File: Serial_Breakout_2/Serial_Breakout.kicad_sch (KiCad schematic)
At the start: 3 parts, among them J1 VIC Serial In, J2 Disc Serial Out, J3 Breakout

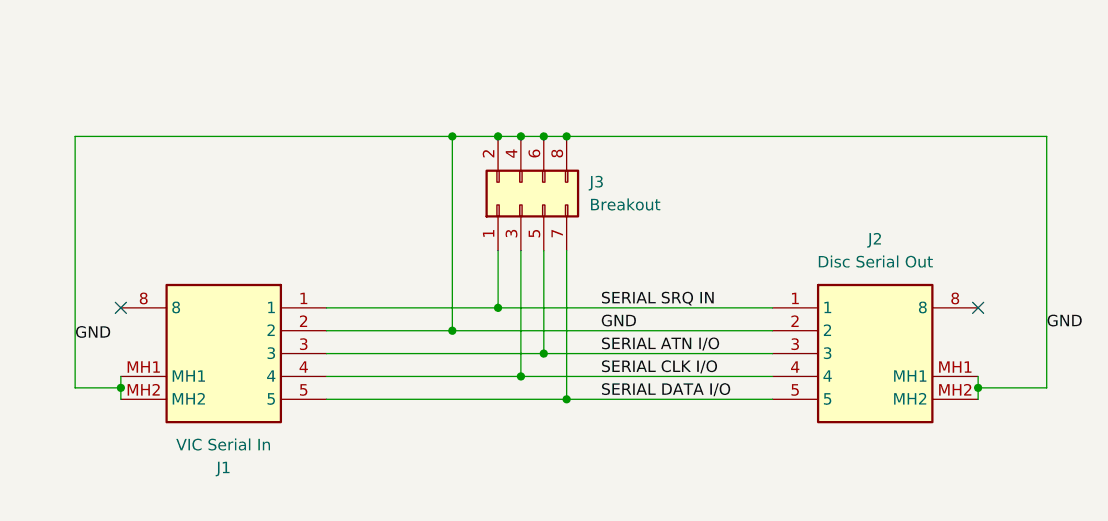
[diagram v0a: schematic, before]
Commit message: Corrected pinout
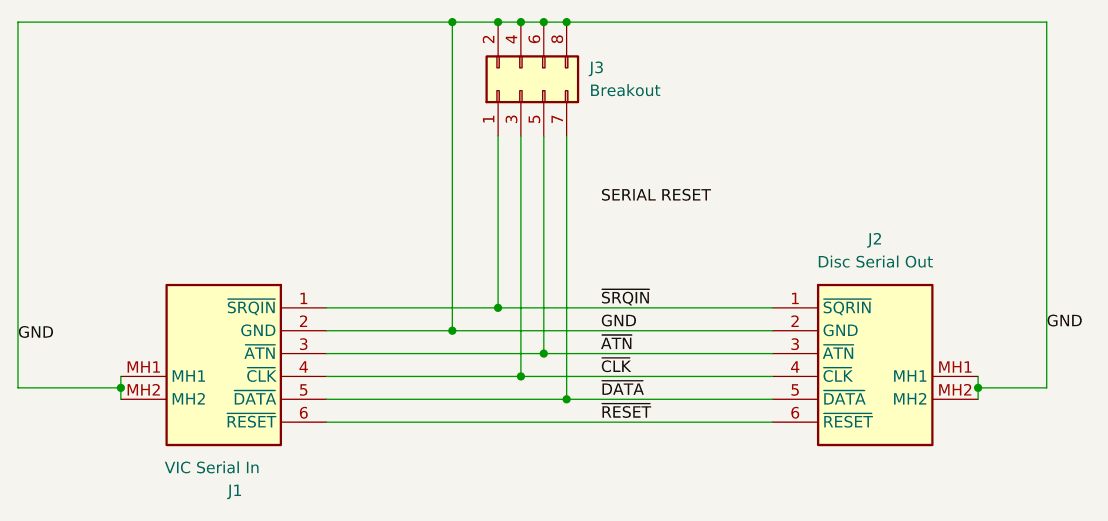
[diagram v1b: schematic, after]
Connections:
- net SERIAL ATN I/O renamed ~{ATN}
- net SERIAL CLK I/O renamed ~{CLK}
- net SERIAL DATA I/O renamed ~{DATA}
- net SERIAL SRQ IN renamed ~{SRQIN}
- new net ~{RESET}: J1.6 (~{RESET}), J2.6 (~{RESET})
- no-connect marks 2 -> 0
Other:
- moved on the sheet: J1, J2, J3
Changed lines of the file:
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@@
 	(title_block
 		(title "Breakout Board for Commodore Serial Port")
-		(date "23/NOV/2025")
-		(rev "B")
+		(date "22/FEB/2026")
+		(rev "C")
 		(company "www.youtube.com/@Brfff")
 	)
@@
 	)
 	(junction
-		(at 82.55 38.1)
-		(diameter 0)
-		(color 0 0 0 0)
-	)
-	(junction
-		(at 85.09 38.1)
-		(diameter 0)
-		(color 0 0 0 0)
-	)
-	(junction
-		(at 77.47 38.1)
-		(diameter 0)
-		(color 0 0 0 0)
-	)
-	(junction
-		(at 90.17 38.1)
+		(at 82.55 25.4)
+		(diameter 0)
+		(color 0 0 0 0)
+	)
+	(junction
+		(at 85.09 25.4)
+		(diameter 0)
+		(color 0 0 0 0)
+	)
+	(junction
+		(at 77.47 25.4)
+		(diameter 0)
+		(color 0 0 0 0)
+	)
+	(junction
+		(at 90.17 25.4)
 		(diameter 0)
 		(color 0 0 0 0)
@@
 	)
 	(junction
-		(at 87.63 38.1)
-		(diameter 0)
-		(color 0 0 0 0)
-	)
-	(no_connect
-		(at 40.64 57.15)
-	)
-	(no_connect
-		(at 135.89 57.15)
-	)
-	(wire
-		(pts
-			(xy 90.17 50.8) (xy 90.17 67.31)
+		(at 87.63 25.4)
+		(diameter 0)
+		(color 0 0 0 0)
+	)
+	(wire
+		(pts
+			(xy 90.17 38.1) (xy 90.17 67.31)
 		)
 		(stroke
@@
 	(wire
 		(pts
-			(xy 82.55 50.8) (xy 82.55 57.15)
+			(xy 82.55 38.1) (xy 82.55 57.15)
 		)
 		(stroke
@@
 	(wire
 		(pts
-			(xy 87.63 38.1) (xy 90.17 38.1)
+			(xy 87.63 25.4) (xy 90.17 25.4)
 		)
 		(stroke
@@
 	(wire
 		(pts
-			(xy 77.47 59.69) (xy 77.47 38.1)
-		)
-		(stroke
-			(width 0)
-			(type default)
-		)
-	)
-	(wire
-		(pts
-			(xy 143.51 38.1) (xy 143.51 66.04)
-		)
-		(stroke
-			(width 0)
-			(type default)
-		)
-	)
-	(wire
-		(pts
-			(xy 40.64 66.04) (xy 35.56 66.04)
-		)
-		(stroke
-			(width 0)
-			(type default)
-		)
-	)
-	(wire
-		(pts
-			(xy 85.09 38.1) (xy 87.63 38.1)
+			(xy 77.47 59.69) (xy 77.47 25.4)
+		)
+		(stroke
+			(width 0)
+			(type default)
+		)
+	)
+	(wire
+		(pts
+			(xy 63.5 69.85) (xy 113.03 69.85)
+		)
+		(stroke
+			(width 0)
+			(type default)
+		)
+	)
+	(wire
+		(pts
+			(xy 143.51 25.4) (xy 143.51 66.04)
+		)
+		(stroke
+			(width 0)
+			(type default)
+		)
+	)
+	(wire
+		(pts
+			(xy 40.64 66.04) (xy 29.21 66.04)
+		)
+		(stroke
+			(width 0)
+			(type default)
+		)
+	)
+	(wire
+		(pts
+			(xy 85.09 25.4) (xy 87.63 25.4)
 		)
 		(stroke
@@
 	(wire
 		(pts
-			(xy 35.56 38.1) (xy 77.47 38.1)
-		)
-		(stroke
-			(width 0)
-			(type default)
-		)
-	)
-	(wire
-		(pts
-			(xy 90.17 38.1) (xy 143.51 38.1)
-		)
-		(stroke
-			(width 0)
-			(type default)
-		)
-	)
-	(wire
-		(pts
-			(xy 87.63 50.8) (xy 87.63 62.23)
+			(xy 29.21 25.4) (xy 77.47 25.4)
+		)
+		(stroke
+			(width 0)
+			(type default)
+		)
+	)
+	(wire
+		(pts
+			(xy 90.17 25.4) (xy 143.51 25.4)
+		)
+		(stroke
+			(width 0)
+			(type default)
+		)
+	)
+	(wire
+		(pts
+			(xy 87.63 38.1) (xy 87.63 62.23)
 		)
 		(stroke
@@
 	(wire
 		(pts
-			(xy 82.55 38.1) (xy 85.09 38.1)
+			(xy 82.55 25.4) (xy 85.09 25.4)
 		)
 		(stroke
@@
 	(wire
 		(pts
-			(xy 35.56 66.04) (xy 35.56 38.1)
+			(xy 29.21 66.04) (xy 29.21 25.4)
 		)
 		(stroke
@@
 	(wire
 		(pts
-			(xy 77.47 38.1) (xy 82.55 38.1)
+			(xy 77.47 25.4) (xy 82.55 25.4)
 		)
 		(stroke
@@
 	(wire
 		(pts
-			(xy 85.09 50.8) (xy 85.09 64.77)
-		)
-		(stroke
-			(width 0)
-			(type default)
-		)
-	)
-	(label "SERIAL SRQ IN"
+			(xy 85.09 38.1) (xy 85.09 64.77)
+		)
+		(stroke
+			(width 0)
+			(type default)
+		)
+	)
+	(label "~{RESET}"
+		(at 93.98 69.85 0)
+		(effects
+			(font
+				(size 1.27 1.27)
+			)
+			(justify left bottom)
+		)
+	)
+	(label "~{SRQIN}"
 		(at 93.98 57.15 0)
 		(effects
@@
 		)
 	)
-	(label "SERIAL ATN I{slash}O"
+	(label "SERIAL RESET"
+		(at 93.98 45.72 0)
+		(effects
+			(font
+				(size 1.27 1.27)
+			)
+			(justify left bottom)
+		)
+	)
+	(label "~{ATN}"
 		(at 93.98 62.23 0)
 		(effects
@@
 		)
 	)
-	(label "SERIAL DATA I{slash}O"
+	(label "~{DATA}"
 		(at 93.98 67.31 0)
 		(effects
@@
 		)
 	)
-	(label "SERIAL CLK I{slash}O"
+	(label "~{CLK}"
 		(at 93.98 64.77 0)
 		(effects
@@
 	)
 	(label "GND"
-		(at 35.56 60.96 0)
+		(at 29.21 60.96 0)
 		(effects
 			(font
@@
 	(symbol
 		(lib_id "Connector_Generic:Conn_02x04_Odd_Even")
-		(at 85.09 45.72 90)
+		(at 85.09 33.02 90)
 		(unit 1)
 		(exclude_from_sim no)
@@
 		(fields_autoplaced yes)
 		(property "Reference" "J3"
-			(at 92.71 43.1799 90)
+			(at 92.71 30.4799 90)
 			(effects
 				(font
@@
 		)
 		(property "Value" "Breakout"
-			(at 92.71 45.7199 90)
+			(at 92.71 33.0199 90)
 			(effects
 				(font
@@
 		)
 		(property "Footprint" "Connector_PinHeader_2.54mm:PinHeader_2x04_P2.54mm_Vertical"
-			(at 85.09 45.72 0)
+			(at 85.09 33.02 0)
 			(effects
 				(font
@@
 		)
 		(property "Datasheet" "~"
-			(at 85.09 45.72 0)
+			(at 85.09 33.02 0)
 			(effects
 				(font
@@
 		)
 		(property "Description" "Generic connector, double row, 02x04, odd/even pin numbering scheme (row 1 odd numbers, row 2 even numbers), script generated (kicad-library-utils/schlib/autogen/connector/)"
-			(at 85.09 45.72 0)
+			(at 85.09 33.02 0)
 			(effects
 				(font
@@
 	)
 	(symbol
+		(lib_name "671-0601_1")
 		(lib_id "Clueless_Engineer:671-0601")
 		(at 63.5 57.15 0)
@@
 		(dnp no)
 		(property "Reference" "J1"
-			(at 52.07 74.93 0)
+			(at 53.34 77.47 0)
 			(effects
 				(font
@@
 		)
 		(property "Value" "VIC Serial In"
-			(at 52.07 72.39 0)
+			(at 50.8 74.93 0)
 			(effects
 				(font
@@
 		(pin "5"
 		)
-		(pin "8"
+		(pin "6"
 		)
 		(pin "MH1"
@@
 		)
 		(property "Description" "Deltron 6 Pole Right Angle Din Socket Socket, 2A, 100 V ac, Lockable"
-			(at 113.03 57.15 0)
+			(at 118.11 77.47 0)
 			(effects
 				(font
@@
 		(pin "5"
 		)
-		(pin "8"
+		(pin "6"
 		)
 		(pin "MH1"
